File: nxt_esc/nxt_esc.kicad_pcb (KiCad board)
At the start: 2 copper layers, 47.6 x 47.6 mm, 18 parts, among them IC1 L293D, J1 NXT_MOTOR, J2 NXT_MOTOR, SW1 Skid Steer/Drive & Steer, SW2 Center Steering, U1 LM7805CT

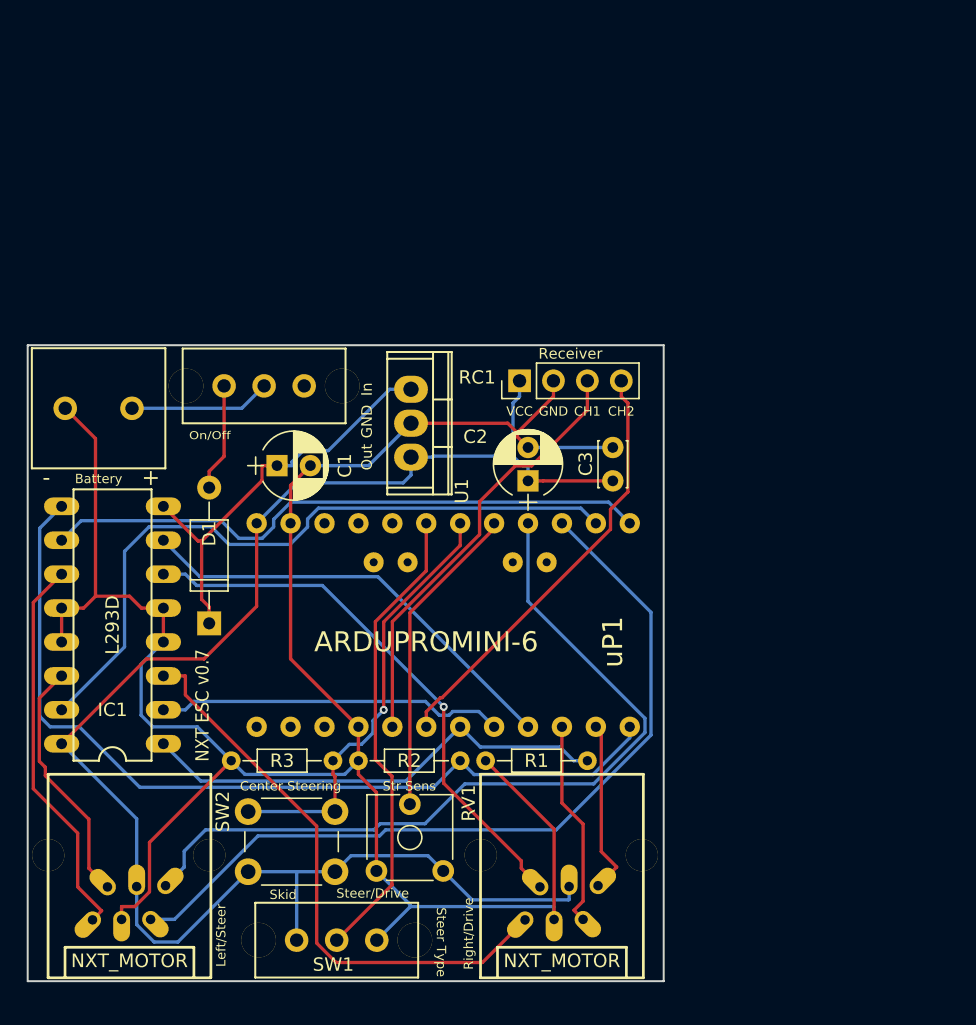
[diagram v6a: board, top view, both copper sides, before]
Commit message: Rotated NXT jacks
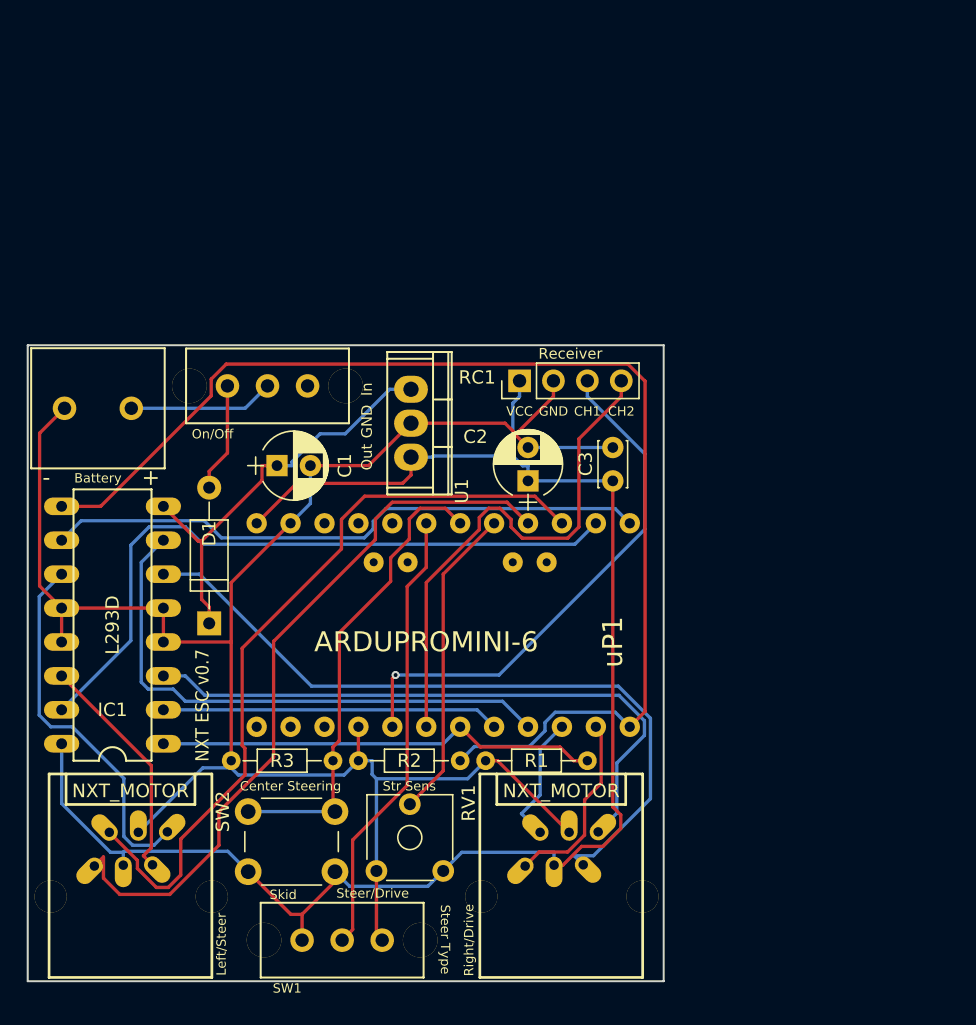
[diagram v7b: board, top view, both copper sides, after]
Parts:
- moved J2 7.09 mm to (118.8, 120.8), turned to 0 degrees
- moved J1 7.09 mm to (151.1, 120.8), turned to 0 degrees
- moved SW1 0.41 mm to (134.7, 122.0)
- moved On/Off 0.25 mm to (129.1, 80.5)
- moved Battery 0.05 mm to (116.4, 82.2)
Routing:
- net Net-(IC1-Pad9): track 66.0 -> 90.7 mm
- net GND: track 165.6 -> 142.9 mm
- net Net-(IC1-Pad6): track 41.6 -> 55.4 mm, vias 1 -> 0
- net Net-(IC1-Pad7): track 33.1 -> 41.7 mm
- net Net-(RC1-Pad3): track 32.7 -> 40.1 mm, vias 0 -> 1
- net Net-(RC1-Pad4): track 32.4 -> 38.9 mm
- net Net-(J1-Pad5): track 15.6 -> 9.74 mm
- net Net-(J2-Pad6): track 60.6 -> 55.1 mm
- net Net-(J2-Pad5): track 61.8 -> 57.7 mm
- net Net-(IC1-Pad3): track 43.3 -> 47.2 mm
- net Net-(R3-Pad2): track 32.6 -> 35.5 mm, vias 1 -> 0
- net Net-(IC1-Pad1): track 35.6 -> 33.3 mm
- net Net-(IC1-Pad11): track 29.2 -> 27.9 mm
- net Net-(IC1-Pad15): track 52.4 -> 51.1 mm
- net Net-(SW1-Pad2): track 35.0 -> 33.8 mm
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
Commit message: Made more room for arduino
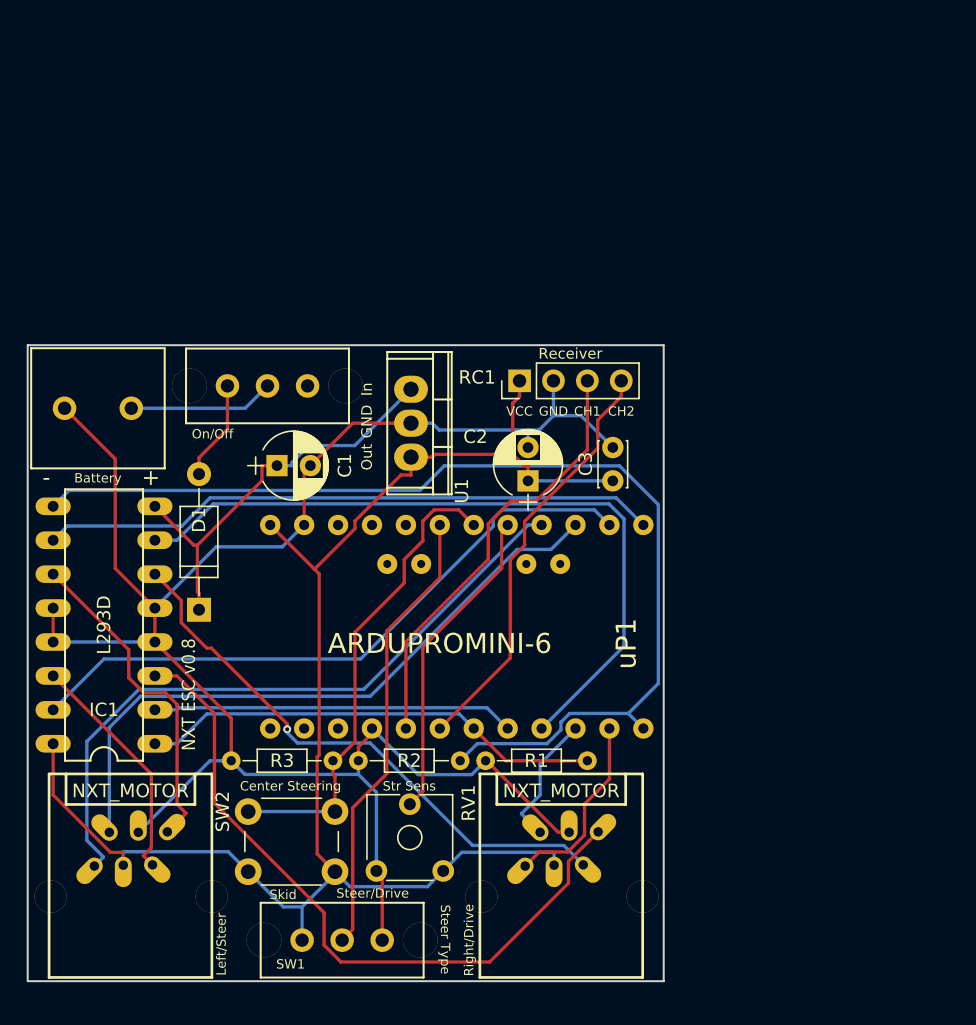
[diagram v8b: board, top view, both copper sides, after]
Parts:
- moved D1 1.27 mm to (124.0, 97.3)
- moved uP1 1.02 mm to (122.9, 108.7)
- moved IC1 0.63 mm to (116.8, 98.4)
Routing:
- net Net-(IC1-Pad7): track 41.7 -> 55.0 mm
- net Net-(IC1-Pad6): track 55.4 -> 42.4 mm, vias 0 -> 1
- net Net-(IC1-Pad9): track 90.7 -> 80.3 mm
- net Net-(J2-Pad5): track 57.7 -> 49.0 mm
- net Net-(RC1-Pad3): track 40.1 -> 32.8 mm, vias 1 -> 0
- net Net-(RC1-Pad4): track 38.9 -> 31.7 mm
- net Net-(C2-Pad1): track 121.2 -> 115.2 mm
- net Net-(IC1-Pad3): track 47.2 -> 52.4 mm
- net Net-(J2-Pad6): track 55.1 -> 50.9 mm
- net Net-(IC1-Pad11): track 27.9 -> 24.9 mm
- net Net-(IC1-Pad15): track 51.1 -> 48.7 mm
- net Net-(IC1-Pad2): track 25.3 -> 27.1 mm
- net GND: track 142.9 -> 144.6 mm
- net Net-(IC1-Pad1): track 33.3 -> 34.8 mm
- net Net-(IC1-Pad10): track 45.4 -> 46.4 mm
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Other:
- board text added: "NXT ESC v0.8"
- board text removed: "NXT ESC v0.7"
